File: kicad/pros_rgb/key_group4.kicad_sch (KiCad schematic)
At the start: 14 parts

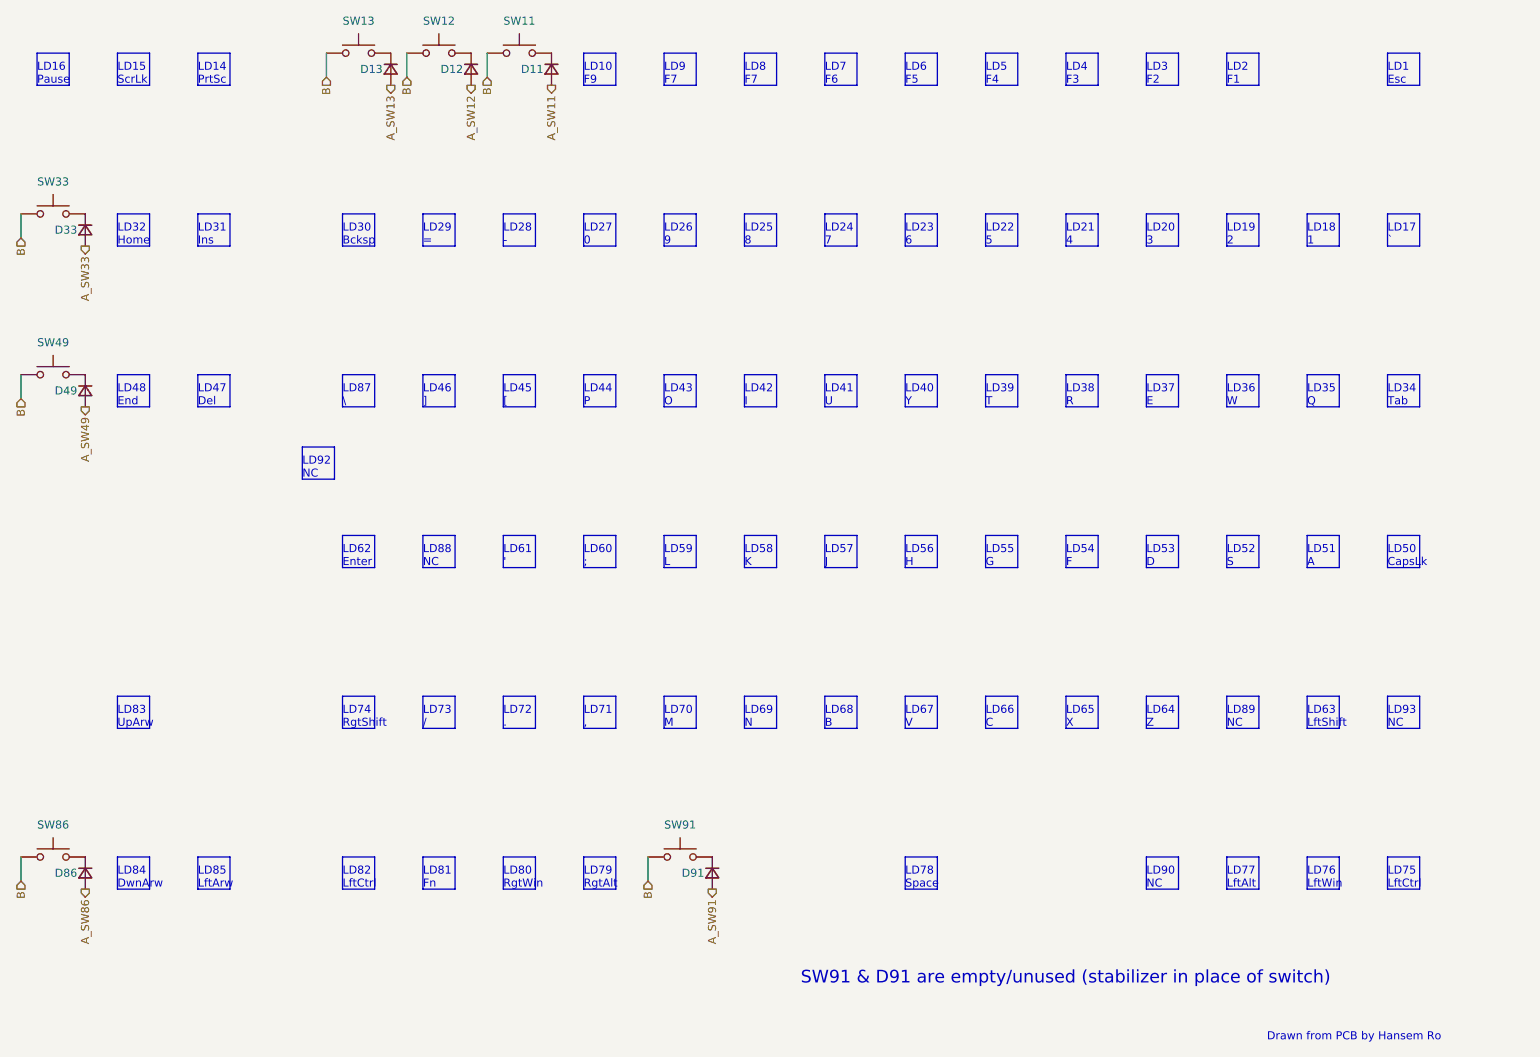
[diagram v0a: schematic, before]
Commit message: kicad/pros_rgb: update key groupings
These new groupings are based off ordering in firmware:
https://github.com/hansemro/pok3r_re_firmware/blob/4b68aa4baf7d28dc8dbf8eebcb1fdb59e7bcd629/disassemble/cmprosrgb/v122/cmprosrgb_v122.txt#L14599-L14629
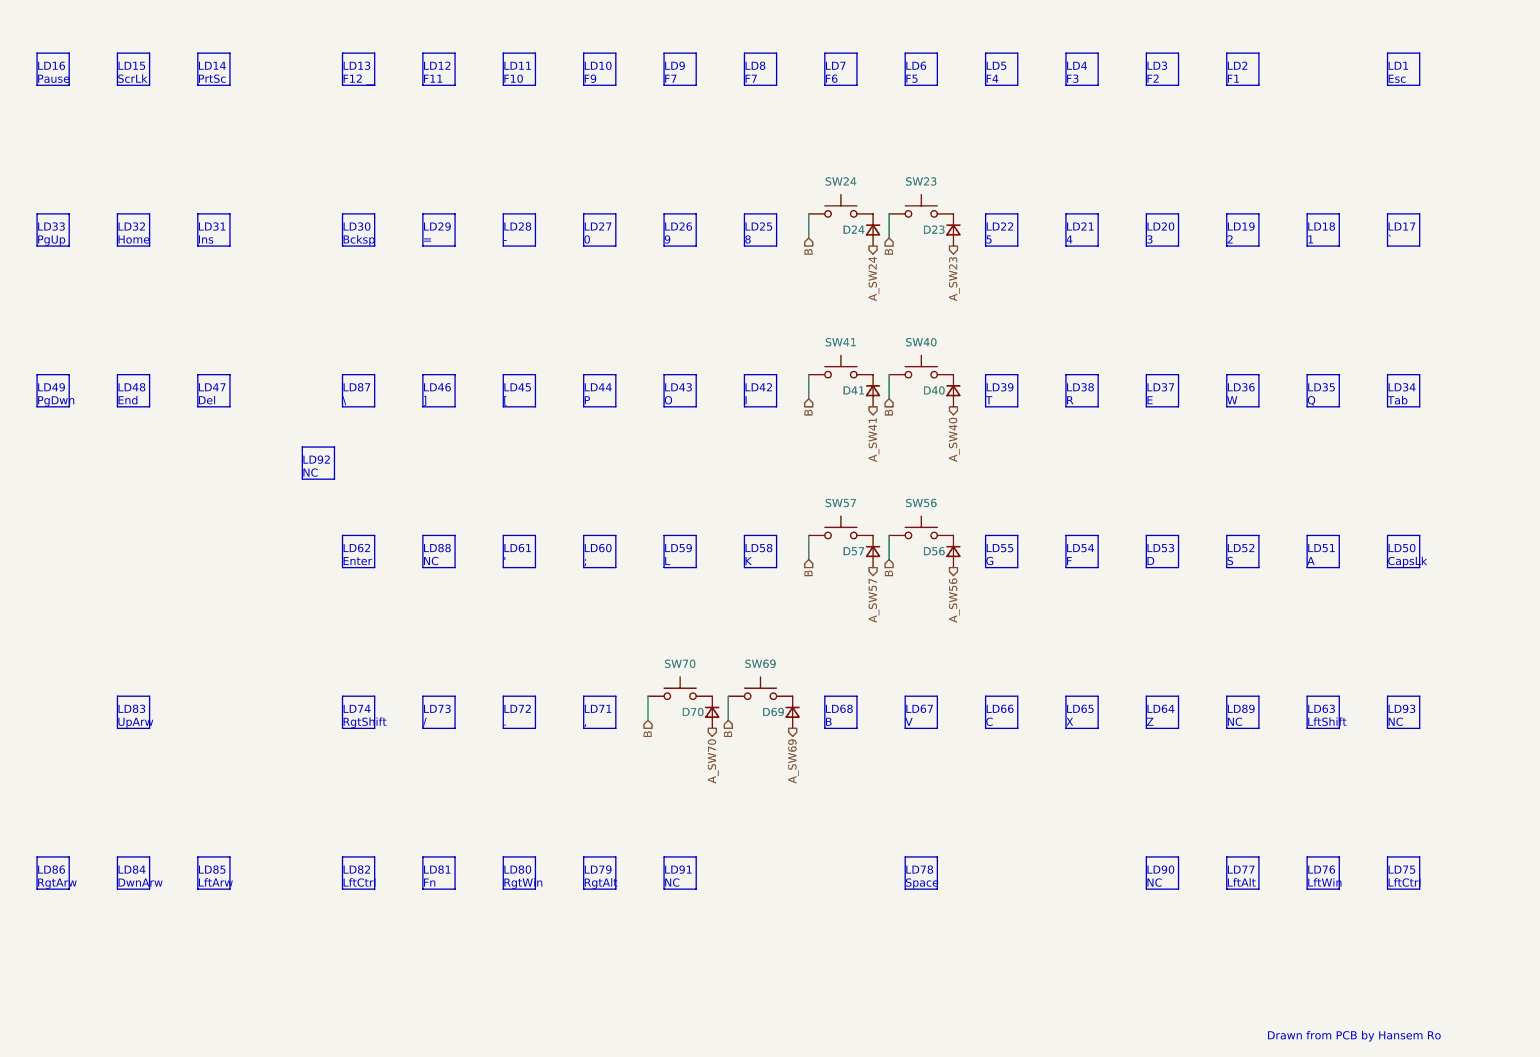
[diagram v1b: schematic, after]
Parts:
- removed D11, D12, D13, D33, D49, D86, D91: ~, symbol Device:D_Small
- removed SW11, SW12, SW13, SW33, SW49, SW86, SW91: ~, symbol Switch:SW_Push
- added D23, D24, D40, D41, D56, D57, D69, D70: (no value), symbol Device:D_Small
- added SW23, SW24, SW40, SW41, SW56, SW57, SW69, SW70: (no value), symbol Switch:SW_Push
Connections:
- net B: now also SW23.1, SW24.1, SW40.1, SW41.1, SW56.1, SW57.1, SW69.1, SW70.1
- new net: D23.1 (K), SW23.2
- new net: D56.1 (K), SW56.2
- new net: D57.1 (K), SW57.2
- new net: D70.1 (K), SW70.2
- new net: D40.1 (K), SW40.2
- new net: D69.1 (K), SW69.2
- new net: D41.1 (K), SW41.2
- new net: D24.1 (K), SW24.2
- new net A_SW23: D23.2 (A)
- new net A_SW24: D24.2 (A)
- new net A_SW40: D40.2 (A)
- new net A_SW41: D41.2 (A)
- new net A_SW56: D56.2 (A)
- new net A_SW57: D57.2 (A)
- new net A_SW69: D69.2 (A)
- new net A_SW70: D70.2 (A)
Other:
- note added: "LD11 F10"
- note added: "LD12 F11"
- note added: "LD13 F12"
- note added: "LD33 PgUp"
- note added: "LD49 PgDwn"
- note added: "LD86 RgtArw"
- note added: "LD91 NC"
- note removed: "LD23 6"
- note removed: "LD24 7"
- note removed: "LD40 Y"
- note removed: "LD41 U"
- note removed: "LD56 H"
- note removed: "LD57 J"
- note removed: "LD69 N"
- note removed: "LD70 M"
- note removed: "SW91 & D91 are empty/unused (stabilizer in place of switch)"

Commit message: kicad/pros_rgb: mark as Rev. B
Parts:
- D23, D24, D40, D41, D56, D57, D69, D70, SW23, SW24, SW40, SW41, SW56, SW57, SW69, SW70: value (none) -> ~
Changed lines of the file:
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@@
     (in_bom yes) (on_board yes)
     (property "Reference" "SW23" (id 0) (at 198.12 44.45 0))
-    (property "Value" "" (id 1) (at 198.12 44.45 0))
+    (property "Value" "~" (id 1) (at 198.12 44.45 0))
     (property "Footprint" "" (id 2) (at 198.12 44.45 0)
       (effects (font (size 1.27 1.27)) hide)
@@
     (in_bom yes) (on_board yes)
     (property "Reference" "SW56" (id 0) (at 198.12 95.25 0))
-    (property "Value" "" (id 1) (at 198.12 95.25 0))
+    (property "Value" "~" (id 1) (at 198.12 95.25 0))
     (property "Footprint" "" (id 2) (at 198.12 95.25 0)
       (effects (font (size 1.27 1.27)) hide)
@@
     (in_bom yes) (on_board yes)
     (property "Reference" "SW57" (id 0) (at 185.42 95.25 0))
-    (property "Value" "" (id 1) (at 185.42 95.25 0))
+    (property "Value" "~" (id 1) (at 185.42 95.25 0))
     (property "Footprint" "" (id 2) (at 185.42 95.25 0)
       (effects (font (size 1.27 1.27)) hide)
@@
     (in_bom yes) (on_board yes)
     (property "Reference" "SW70" (id 0) (at 160.02 120.65 0))
-    (property "Value" "" (id 1) (at 160.02 120.65 0))
+    (property "Value" "~" (id 1) (at 160.02 120.65 0))
     (property "Footprint" "" (id 2) (at 160.02 120.65 0)
       (effects (font (size 1.27 1.27)) hide)
@@
     (in_bom yes) (on_board yes)
     (property "Reference" "SW40" (id 0) (at 198.12 69.85 0))
-    (property "Value" "" (id 1) (at 198.12 69.85 0))
+    (property "Value" "~" (id 1) (at 198.12 69.85 0))
     (property "Footprint" "" (id 2) (at 198.12 69.85 0)
       (effects (font (size 1.27 1.27)) hide)
@@
     (in_bom yes) (on_board yes)
     (property "Reference" "SW69" (id 0) (at 172.72 120.65 0))
-    (property "Value" "" (id 1) (at 172.72 120.65 0))
+    (property "Value" "~" (id 1) (at 172.72 120.65 0))
     (property "Footprint" "" (id 2) (at 172.72 120.65 0)
       (effects (font (size 1.27 1.27)) hide)
@@
       (effects (font (size 1.27 1.27)) (justify right))
     )
-    (property "Value" "" (id 1) (at 205.74 78.7399 90)
+    (property "Value" "~" (id 1) (at 205.74 78.7399 90)
       (effects (font (size 1.27 1.27)) (justify left))
     )
@@
     (in_bom yes) (on_board yes)
     (property "Reference" "SW41" (id 0) (at 185.42 69.85 0))
-    (property "Value" "" (id 1) (at 185.42 69.85 0))
+    (property "Value" "~" (id 1) (at 185.42 69.85 0))
     (property "Footprint" "" (id 2) (at 185.42 69.85 0)
       (effects (font (size 1.27 1.27)) hide)
@@
       (effects (font (size 1.27 1.27)) (justify right))
     )
-    (property "Value" "" (id 1) (at 180.34 129.5399 90)
+    (property "Value" "~" (id 1) (at 180.34 129.5399 90)
       (effects (font (size 1.27 1.27)) (justify left))
     )
@@
       (effects (font (size 1.27 1.27)) (justify right))
     )
-    (property "Value" "" (id 1) (at 205.74 104.1399 90)
+    (property "Value" "~" (id 1) (at 205.74 104.1399 90)
       (effects (font (size 1.27 1.27)) (justify left))
     )
@@
     (in_bom yes) (on_board yes)
     (property "Reference" "SW24" (id 0) (at 185.42 44.45 0))
-    (property "Value" "" (id 1) (at 185.42 44.45 0))
+    (property "Value" "~" (id 1) (at 185.42 44.45 0))
     (property "Footprint" "" (id 2) (at 185.42 44.45 0)
       (effects (font (size 1.27 1.27)) hide)
@@
       (effects (font (size 1.27 1.27)) (justify right))
     )
-    (property "Value" "" (id 1) (at 193.04 78.7399 90)
+    (property "Value" "~" (id 1) (at 193.04 78.7399 90)
       (effects (font (size 1.27 1.27)) (justify left))
     )
@@
       (effects (font (size 1.27 1.27)) (justify right))
     )
-    (property "Value" "" (id 1) (at 193.04 53.3399 90)
+    (property "Value" "~" (id 1) (at 193.04 53.3399 90)
       (effects (font (size 1.27 1.27)) (justify left))
     )
@@
       (effects (font (size 1.27 1.27)) (justify right))
     )
-    (property "Value" "" (id 1) (at 167.64 129.5399 90)
+    (property "Value" "~" (id 1) (at 167.64 129.5399 90)
       (effects (font (size 1.27 1.27)) (justify left))
     )
@@
       (effects (font (size 1.27 1.27)) (justify right))
     )
-    (property "Value" "" (id 1) (at 193.04 104.1399 90)
+    (property "Value" "~" (id 1) (at 193.04 104.1399 90)
       (effects (font (size 1.27 1.27)) (justify left))
     )
@@
       (effects (font (size 1.27 1.27)) (justify right))
     )
-    (property "Value" "" (id 1) (at 205.74 53.3399 90)
-      (effects (font (size 1.27 1.27)) (justify left))
-    )
+    (property "Value" "~" (id 1) (at 205.74 53.3399 90)
+      (effects (font (size 1.27 1.27)) (justify left))
+    )

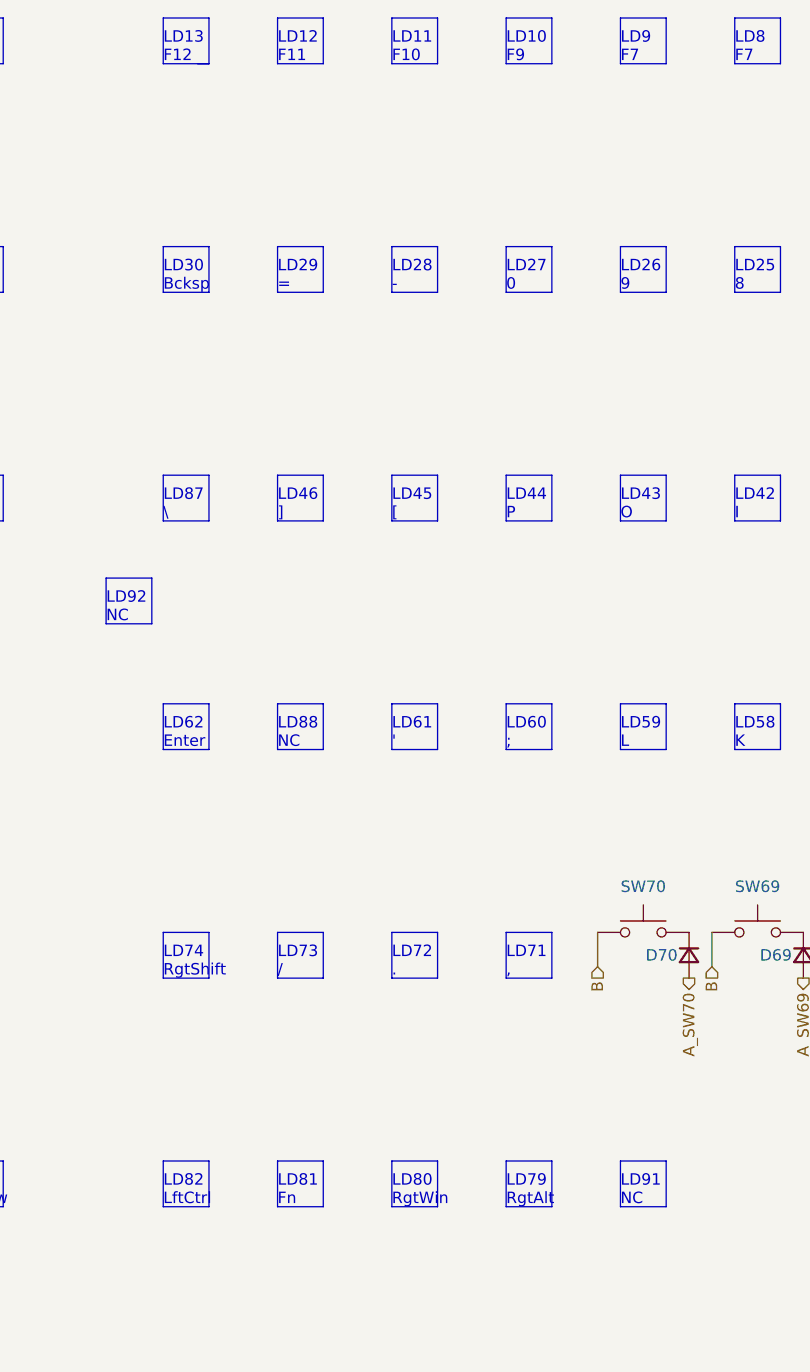
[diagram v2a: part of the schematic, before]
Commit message: kicad/pros_rgb: fix typos
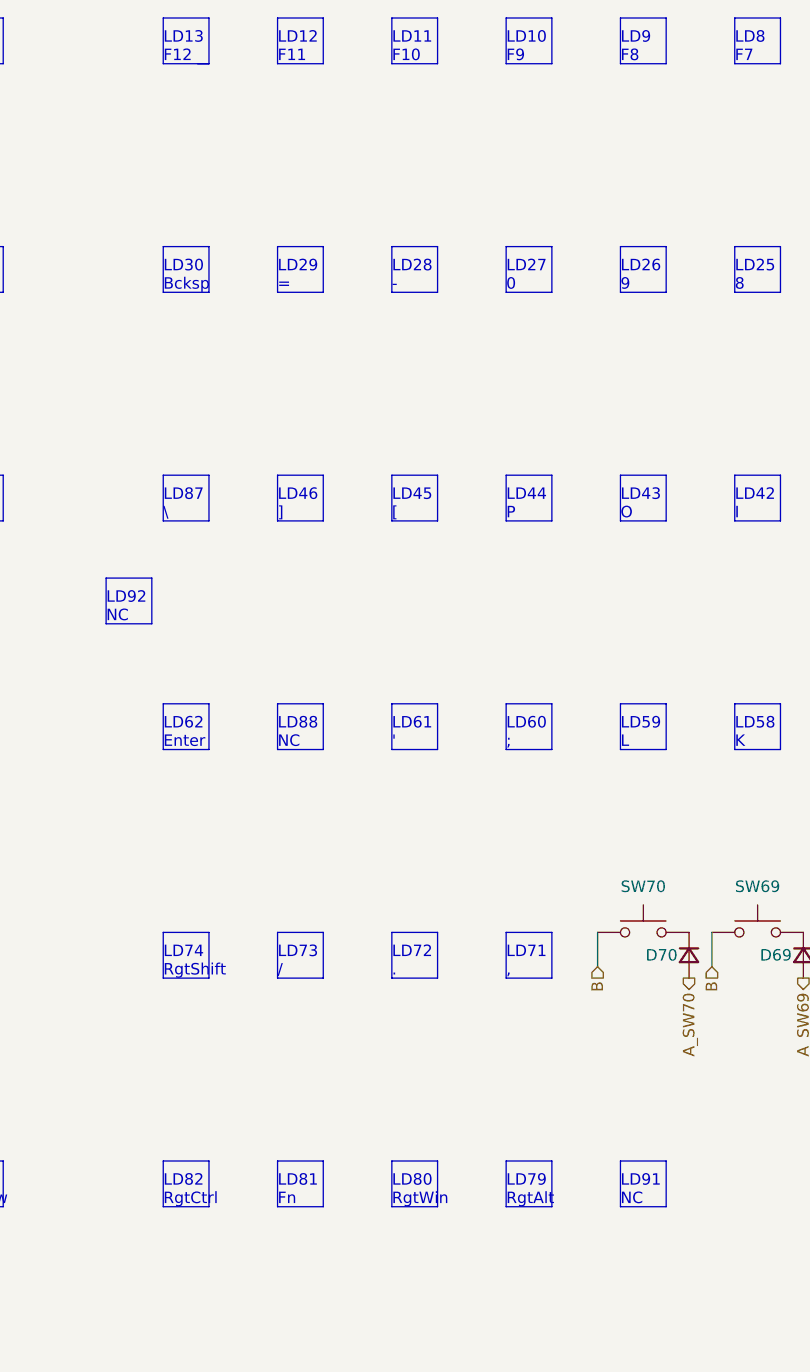
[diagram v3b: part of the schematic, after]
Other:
- note added: "LD82 RgtCtrl"
- note added: "LD9 F8"
- note removed: "LD82 LftCtrl"
- note removed: "LD9 F7"
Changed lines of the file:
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@@
     (effects (font (size 1.27 1.27)) (justify left bottom))
   )
-  (text "LD9\nF7" (at 157.48 29.21 0)
+  (text "LD9\nF8" (at 157.48 29.21 0)
     (effects (font (size 1.27 1.27)) (justify left bottom))
   )
@@
     (effects (font (size 1.27 1.27)) (justify left bottom))
   )
-  (text "LD82\nLftCtrl" (at 106.68 156.21 0)
+  (text "LD82\nRgtCtrl" (at 106.68 156.21 0)
     (effects (font (size 1.27 1.27)) (justify left bottom))
   )
